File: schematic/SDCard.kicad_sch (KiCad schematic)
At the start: 0 parts

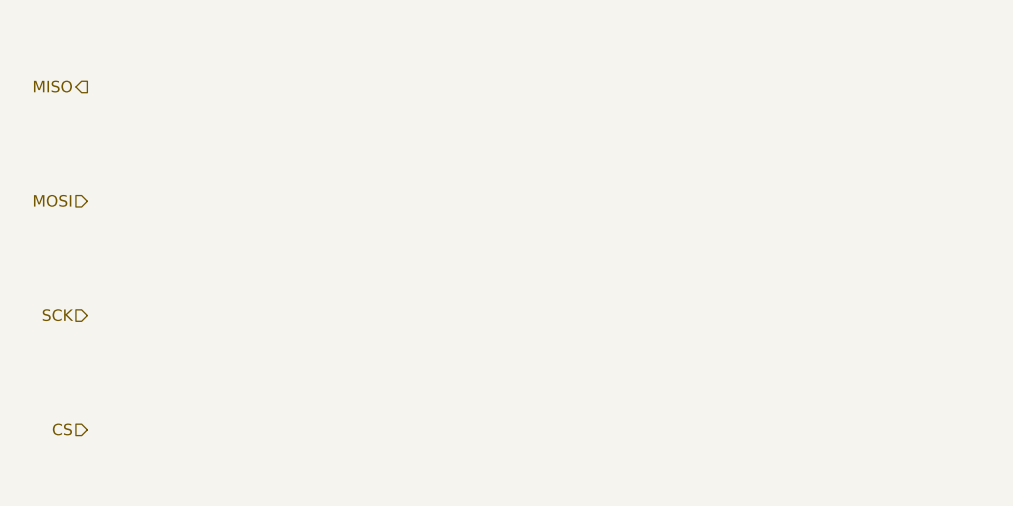
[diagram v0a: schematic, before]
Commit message: Create SD card schematic
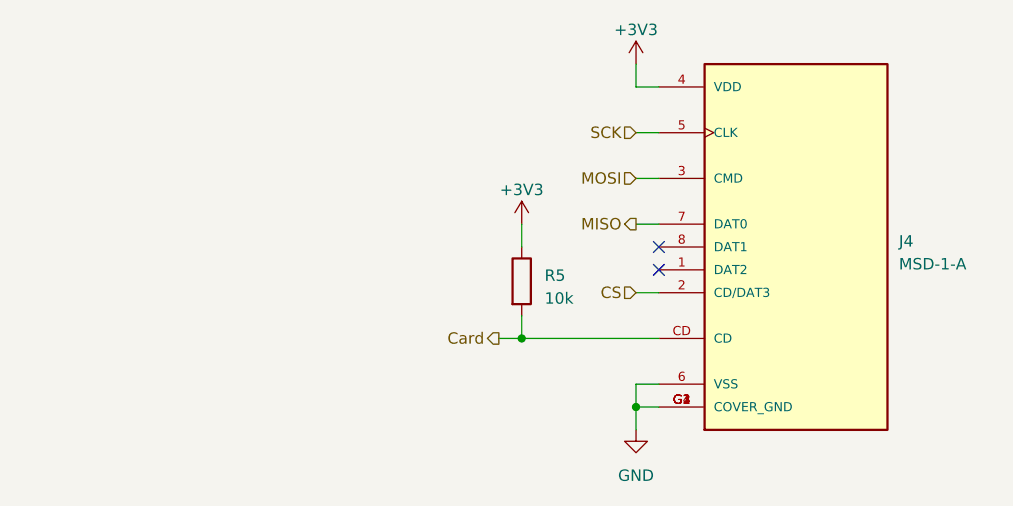
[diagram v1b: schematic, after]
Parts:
- added J4: MSD-1-A, MSD-1-A:CUI_MSD-1-A, symbol MSD-1-A:MSD-1-A
- added R5: 10k, symbol Device:R
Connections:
- net CS: now also J4.2 (CD/DAT3)
- net MISO: now also J4.7 (DAT0)
- net MOSI: now also J4.3 (CMD)
- net SCK: now also J4.5 (CLK)
- new net +3V3: J4.4 (VDD), R5.1
- new net Card: J4.CD, R5.2
- new net GND: J4.6 (VSS), J4.G1 (COVER_GND), J4.G2 (COVER_GND), J4.G3 (COVER_GND), J4.G4 (COVER_GND)
- no-connect marks 0 -> 2
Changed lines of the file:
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@@
 (kicad_sch (version 20230121) (generator eeschema)
   (paper "A4")
-  (hierarchical_label "SCK" (shape input) (at 101.6 101.6 180) (fields_autoplaced)
-    (effects (font (size 1.27 1.27)) (justify right))
-  )
-  (hierarchical_label "MOSI" (shape input) (at 101.6 88.9 180) (fields_autoplaced)
-    (effects (font (size 1.27 1.27)) (justify right))
-  )
-  (hierarchical_label "MISO" (shape output) (at 101.6 76.2 180) (fields_autoplaced)
-    (effects (font (size 1.27 1.27)) (justify right))
-  )
-  (hierarchical_label "CS" (shape input) (at 101.6 114.3 180) (fields_autoplaced)
-    (effects (font (size 1.27 1.27)) (justify right))
+  (junction (at 162.56 111.76) (diameter 0) (color 0 0 0 0)
+  )
+  (junction (at 149.86 104.14) (diameter 0) (color 0 0 0 0)
+  )
+  (no_connect (at 165.1 96.52))
+  (no_connect (at 165.1 93.98))
+  (wire (pts (xy 162.56 111.76) (xy 165.1 111.76))
+    (stroke (width 0) (type default))
+  )
+  (wire (pts (xy 149.86 104.14) (xy 165.1 104.14))
+    (stroke (width 0) (type default))
+  )
+  (wire (pts (xy 162.56 81.28) (xy 165.1 81.28))
+    (stroke (width 0) (type default))
+  )
+  (wire (pts (xy 162.56 111.76) (xy 162.56 109.22))
+    (stroke (width 0) (type default))
+  )
+  (wire (pts (xy 162.56 114.3) (xy 162.56 111.76))
+    (stroke (width 0) (type default))
+  )
+  (wire (pts (xy 149.86 91.44) (xy 149.86 93.98))
+    (stroke (width 0) (type default))
+  )
+  (wire (pts (xy 162.56 109.22) (xy 165.1 109.22))
+    (stroke (width 0) (type default))
+  )
+  (wire (pts (xy 162.56 99.06) (xy 165.1 99.06))
+    (stroke (width 0) (type default))
+  )
+  (wire (pts (xy 147.32 104.14) (xy 149.86 104.14))
+    (stroke (width 0) (type default))
+  )
+  (wire (pts (xy 162.56 86.36) (xy 165.1 86.36))
+    (stroke (width 0) (type default))
+  )
+  (wire (pts (xy 162.56 73.66) (xy 162.56 76.2))
+    (stroke (width 0) (type default))
+  )
+  (wire (pts (xy 162.56 76.2) (xy 165.1 76.2))
+    (stroke (width 0) (type default))
+  )
+  (wire (pts (xy 149.86 104.14) (xy 149.86 101.6))
+    (stroke (width 0) (type default))
+  )
+  (wire (pts (xy 162.56 91.44) (xy 165.1 91.44))
+    (stroke (width 0) (type default))
+  )
+  (hierarchical_label "SCK" (shape input) (at 162.56 81.28 180) (fields_autoplaced)
+    (effects (font (size 1.27 1.27)) (justify right))
+  )
+  (hierarchical_label "MOSI" (shape input) (at 162.56 86.36 180) (fields_autoplaced)
+    (effects (font (size 1.27 1.27)) (justify right))
+  )
+  (hierarchical_label "MISO" (shape output) (at 162.56 91.44 180) (fields_autoplaced)
+    (effects (font (size 1.27 1.27)) (justify right))
+  )
+  (hierarchical_label "Card" (shape output) (at 147.32 104.14 180) (fields_autoplaced)
+    (effects (font (size 1.27 1.27)) (justify right))
+  )
+  (hierarchical_label "CS" (shape input) (at 162.56 99.06 180) (fields_autoplaced)
+    (effects (font (size 1.27 1.27)) (justify right))
+  )
+  (symbol (lib_id "power:+3V3") (at 149.86 91.44 0) (unit 1)
+    (in_bom yes) (on_board yes) (dnp no) (fields_autoplaced)
+    (property "Reference" "#PWR032" (at 149.86 95.25 0)
+      (effects (font (size 1.27 1.27)) hide)
+    )
+    (property "Value" "+3V3" (at 149.86 87.63 0)
+      (effects (font (size 1.27 1.27)))
+    )
+    (property "Footprint" "" (at 149.86 91.44 0)
+      (effects (font (size 1.27 1.27)) hide)
+    )
+    (property "Datasheet" "" (at 149.86 91.44 0)
+      (effects (font (size 1.27 1.27)) hide)
+    )
+    (pin "1")
+    (instances
+      (project "uTesla"
+        (path "/0cecab2b-a552-4f9c-b012-66fc2b7d8bdb/af7f4b01-4906-497f-8eac-258d9974f619"
+          (reference "#PWR032") (unit 1)
+        )
+      )
+    )
+  )
+  (symbol (lib_id "MSD-1-A:MSD-1-A") (at 180.34 93.98 0) (unit 1)
+    (in_bom yes) (on_board yes) (dnp no) (fields_autoplaced)
+    (property "Reference" "J4" (at 191.77 93.345 0)
+      (effects (font (size 1.27 1.27)) (justify left))
+    )
+    (property "Value" "MSD-1-A" (at 191.77 95.885 0)
+      (effects (font (size 1.27 1.27)) (justify left))
+    )
+    (property "Footprint" "MSD-1-A:CUI_MSD-1-A" (at 180.34 93.98 0)
+      (effects (font (size 1.27 1.27)) (justify bottom) hide)
+    )
+    (property "Datasheet" "" (at 180.34 93.98 0)
+      (effects (font (size 1.27 1.27)) hide)
+    )
+    (property "MF" "CUI Devices" (at 180.34 93.98 0)
+      (effects (font (size 1.27 1.27)) (justify bottom) hide)
+    )
+    (property "MAXIMUM_PACKAGE_HEIGHT" "2.00mm" (at 180.34 93.98 0)
+      (effects (font (size 1.27 1.27)) (justify bottom) hide)
+    )
+    (property "Package" "None" (at 180.34 93.98 0)
+      (effects (font (size 1.27 1.27)) (justify bottom) hide)
+    )
+    (property "Price" "None" (at 180.34 93.98 0)
+      (effects (font (size 1.27 1.27)) (justify bottom) hide)
+    )
+    (property "Check_prices" "https://www.snapeda.com/parts/MSD-1-A/CUI+Devices/view-part/?ref=eda" (at 180.34 93.98 0)
+      (effects (font (size 1.27 1.27)) (justify bottom) hide)
+    )
+    (property "STANDARD" "Manufacturer Recommendations" (at 180.34 93.98 0)
+      (effects (font (size 1.27 1.27)) (justify bottom) hide)
+    )
+    (property "PARTREV" "1.0" (at 180.34 93.98 0)
+      (effects (font (size 1.27 1.27)) (justify bottom) hide)
+    )
+    (property "SnapEDA_Link" "https://www.snapeda.com/parts/MSD-1-A/CUI+Devices/view-part/?ref=snap" (at 180.34 93.98 0)
+      (effects (font (size 1.27 1.27)) (justify bottom) hide)
+    )
+    (property "MP" "MSD-1-A" (at 180.34 93.98 0)
+      (effects (font (size 1.27 1.27)) (justify bottom) hide)
+    )
+    (property "Purchase-URL" "https://www.snapeda.com/api/url_track_click_mouser/?unipart_id=15689680&manufacturer=CUI Devices&part_name=MSD-1-A&search_term=None" (at 180.34 93.98 0)
+      (effects (font (size 1.27 1.27)) (justify bottom) hide)
+    )
+    (property "Description" "Micro SD Card Connector, 9 Positions, Connector and Ejector, Push In, Auto Eject Out, Surface Mount, 1.8 mm Height Above Board, Gold Flash" (at 180.34 93.98 0)
+      (effects (font (size 1.27 1.27)) (justify bottom) hide)
+    )
+    (property "CUI_purchase_URL" "https://www.cuidevices.com/product/interconnect/connectors/memory-card-connectors/sd-card-connectors/msd-1-a?utm_source=snapeda.com&utm_medium=referral&utm_campaign=snapedaBOM" (at 180.34 93.98 0)
+      (effects (font (size 1.27 1.27)) (justify bottom) hide)
+    )
+    (property "Availability" "In Stock" (at 180.34 93.98 0)
+      (effects (font (size 1.27 1.27)) (justify bottom) hide)
+    )
+    (property "MANUFACTURER" "CUI Devices" (at 180.34 93.98 0)
+      (effects (font (size 1.27 1.27)) (justify bottom) hide)
+    )
+    (pin "1")
+    (pin "2")
+    (pin "3")
+    (pin "4")
+    (pin "5")
+    (pin "6")
+    (pin "7")
+    (pin "8")
+    (pin "CD")
+    (pin "G1")
+    (pin "G2")
+    (pin "G3")
+    (pin "G4")
+    (instances
+      (project "uTesla"
+        (path "/0cecab2b-a552-4f9c-b012-66fc2b7d8bdb/af7f4b01-4906-497f-8eac-258d9974f619"
+          (reference "J4") (unit 1)
+        )
+      )
+    )
+  )
+  (symbol (lib_id "Device:R") (at 149.86 97.79 0) (unit 1)
+    (in_bom yes) (on_board yes) (dnp no) (fields_autoplaced)
+    (property "Reference" "R5" (at 152.4 97.155 0)
+      (effects (font (size 1.27 1.27)) (justify left))
+    )
+    (property "Value" "10k" (at 152.4 99.695 0)
+      (effects (font (size 1.27 1.27)) (justify left))
+    )
+    (property "Footprint" "" (at 148.082 97.79 90)
+      (effects (font (size 1.27 1.27)) hide)
+    )
+    (property "Datasheet" "~" (at 149.86 97.79 0)
+      (effects (font (size 1.27 1.27)) hide)
+    )
+    (pin "1")
+    (pin "2")
+    (instances
+      (project "uTesla"
+        (path "/0cecab2b-a552-4f9c-b012-66fc2b7d8bdb/af7f4b01-4906-497f-8eac-258d9974f619"
+          (reference "R5") (unit 1)
+        )
+      )
+    )
+  )
+  (symbol (lib_id "power:GND") (at 162.56 114.3 0) (unit 1)
+    (in_bom yes) (on_board yes) (dnp no) (fields_autoplaced)
+    (property "Reference" "#PWR031" (at 162.56 120.65 0)
+      (effects (font (size 1.27 1.27)) hide)
+    )
+    (property "Value" "GND" (at 162.56 119.38 0)
+      (effects (font (size 1.27 1.27)))
+    )
+    (property "Footprint" "" (at 162.56 114.3 0)
+      (effects (font (size 1.27 1.27)) hide)
+    )
+    (property "Datasheet" "" (at 162.56 114.3 0)
+      (effects (font (size 1.27 1.27)) hide)
+    )
+    (pin "1")
+    (instances
+      (project "uTesla"
+        (path "/0cecab2b-a552-4f9c-b012-66fc2b7d8bdb/af7f4b01-4906-497f-8eac-258d9974f619"
+          (reference "#PWR031") (unit 1)
+        )
+      )
+    )
+  )
+  (symbol (lib_id "power:+3V3") (at 162.56 73.66 0) (unit 1)
+    (in_bom yes) (on_board yes) (dnp no) (fields_autoplaced)
+    (property "Reference" "#PWR030" (at 162.56 77.47 0)
+      (effects (font (size 1.27 1.27)) hide)
+    )
+    (property "Value" "+3V3" (at 162.56 69.85 0)
+      (effects (font (size 1.27 1.27)))
+    )
+    (property "Footprint" "" (at 162.56 73.66 0)
+      (effects (font (size 1.27 1.27)) hide)
+    )
+    (property "Datasheet" "" (at 162.56 73.66 0)
+      (effects (font (size 1.27 1.27)) hide)
+    )
+    (pin "1")
+    (instances
+      (project "uTesla"
+        (path "/0cecab2b-a552-4f9c-b012-66fc2b7d8bdb/af7f4b01-4906-497f-8eac-258d9974f619"
+          (reference "#PWR030") (unit 1)
+        )
+      )
+    )
   )
 )

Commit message: Assign footprints
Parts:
- R5: footprint (none) -> Resistor_SMD:R_0603_1608Metric
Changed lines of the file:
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@@
       (effects (font (size 1.27 1.27)) (justify left))
     )
-    (property "Footprint" "" (at 148.082 97.79 90)
+    (property "Footprint" "Resistor_SMD:R_0603_1608Metric" (at 148.082 97.79 90)
       (effects (font (size 1.27 1.27)) hide)
     )
